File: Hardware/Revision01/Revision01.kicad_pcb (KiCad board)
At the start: 4 copper layers, 100 x 110.1 mm, 91 parts, among them J1 CANBUS backup, J10 StrainConn, J11 StrainConn, J12 StrainConn, J2 Conn_01x02, J3 Conn_01x02, J4 Battery connector, J5 StrainConn, J6 StrainConn, J7 StrainConn, J8 StrainConn, J9 StrainConn, Q1 PMOS, Q2 NMOS, Q3 PMOS, SW1 ON/OFF_SW_SPST_LED, U1 NUCLEO-L476RG, U2 MRF89XAM9AT-I/RM, U3 ICM-45605

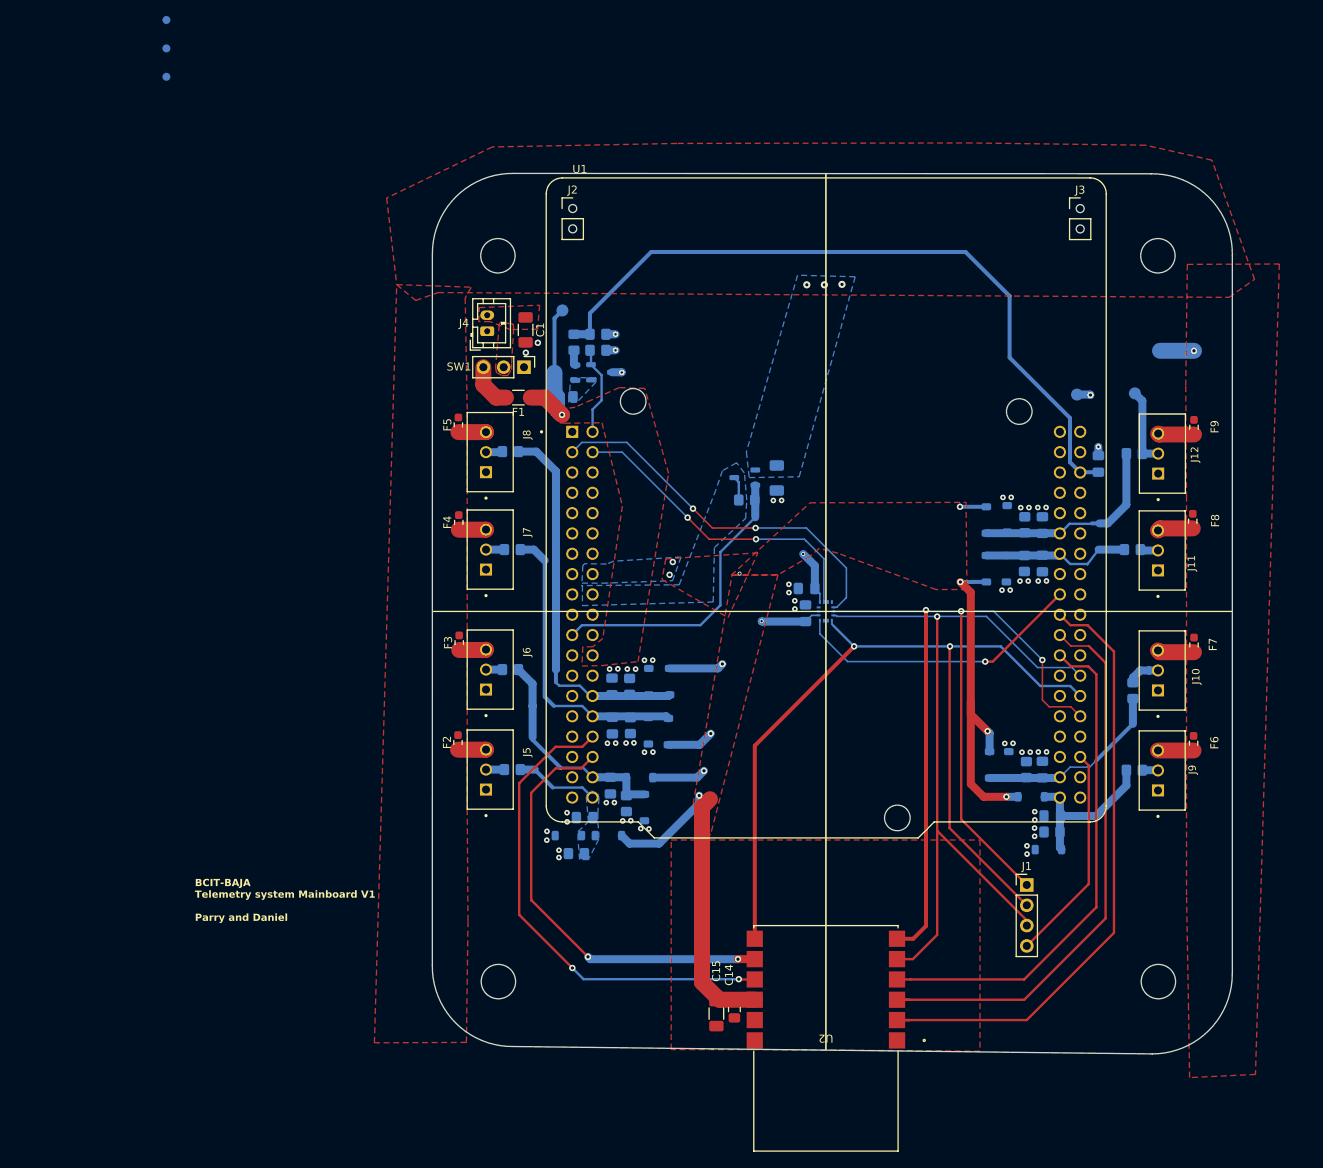
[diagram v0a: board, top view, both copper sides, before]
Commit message: redid ROUTING. Need to redefine layer stackup and stitching via length
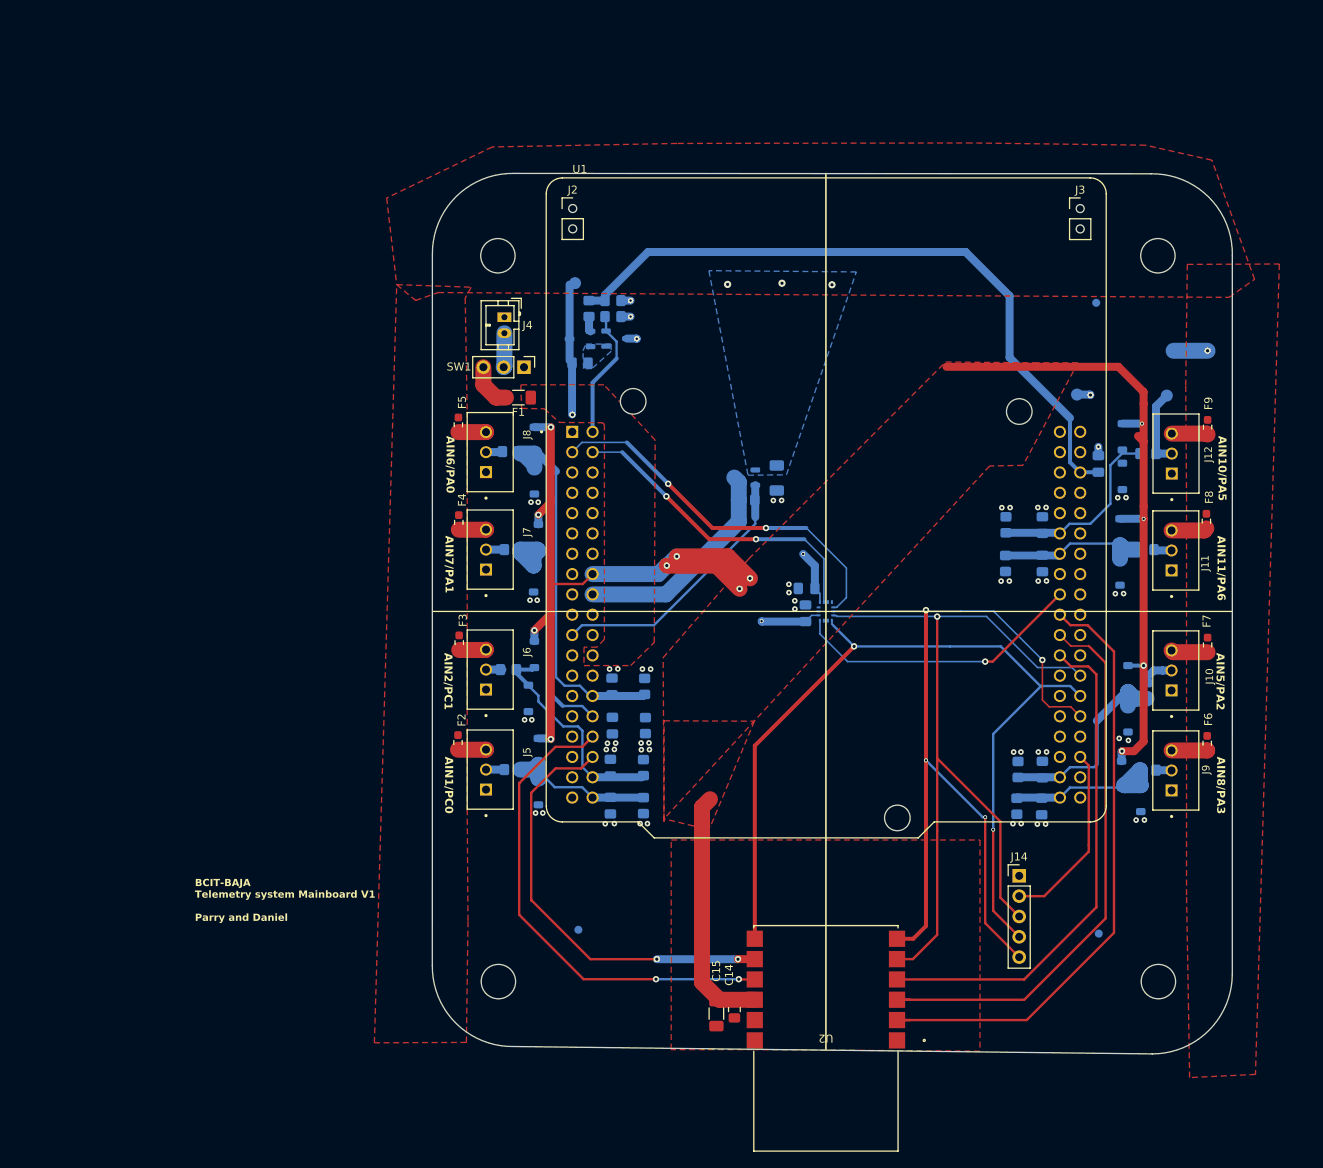
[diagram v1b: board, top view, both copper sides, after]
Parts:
- removed C1: 10uF, Capacitor_SMD:C_1206_3216Metric_Pad1.33x1.80mm_HandSolder
- removed J1: CANBUS backup, Connector_PinHeader_2.54mm:PinHeader_1x04_P2.54mm_Vertical
- added J14: Conn_01x05, Connector_PinHeader_2.54mm:PinHeader_1x05_P2.54mm_Vertical, F.Cu at (184.4, 130.5)
- moved FID2 160.7 mm to (194.3, 137.7)
- moved FID1 121.5 mm to (194.0, 58.8)
- moved FID3 118.4 mm to (129.3, 137.2)
- moved D7 34.6 mm to (123.8, 76.0)
- moved D5 29.2 mm to (124.3, 88.2), turned to -90 degrees
- moved D8 28.9 mm to (123.8, 81.1), turned to -90 degrees
- moved D6 23.8 mm to (123.7, 93.3)
- moved D11 20.4 mm to (198.0, 105.8)
- moved D3 20.3 mm to (123.8, 102.8), turned to -90 degrees
- moved D15 19.9 mm to (197.3, 75.6)
- moved D4 19.9 mm to (123.0, 108.3)
- moved D13 17.3 mm to (197.0, 87.5), turned to -90 degrees
- moved D12 16.0 mm to (198.0, 110.8), turned to -90 degrees
- moved D16 15.3 mm to (197.3, 80.5), turned to -90 degrees
- moved D14 14.2 mm to (197.0, 92.5)
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- renumbered TP10 to +StrainV, TP3 to +Vbatt, TP9 to AIN10, TP8 to GND
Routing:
- net +3.3V: track 124.0 -> 216.1 mm, vias 13 -> 14
- net /PC5_AIN2_14_BATT_V: track 90.5 -> 125.1 mm
- net +5V: track 3.03 -> 27.8 mm
- net /AIN1_1: track 10.5 -> 19.7 mm
- net /PB13_SPI2_SCK: track 120.7 -> 112.7 mm, vias 3 -> 4
- net /PB15_SPI2_MOSI: track 96.6 -> 104.1 mm
- net /BatteryV_Div_Enable_GPIO: track 11.3 -> 16.3 mm
- net /AIN1_7: track 37.2 -> 32.5 mm
- net Net-(BT1-+): track 0.00 -> 4.29 mm
- net /~{CANBUS_CS_GPIO}: track 27.3 -> 23.6 mm
- net /StrainV_Enable_GPIO: track 36.9 -> 33.5 mm
- net /AIN1_6: track 47.1 -> 50.2 mm
- net +V_batt: track 18.7 -> 17.2 mm
- net /AIN1_10: track 25.2 -> 23.8 mm
- net /AIN1_5: track 24.4 -> 25.7 mm
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- removed copper zone on B.Cu, net +3.3V
- removed copper zone on B.Cu, net +5V
- removed copper zone on B.Cu, net /AIN1_1
- removed copper zone on F.Cu, net Net-(BT1-+)
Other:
- board text added: "AIN1/PC0"
- board text added: "AIN10/PA5"
- board text added: "AIN11/PA6"
- board text added: "AIN2/PC1"
- board text added: "AIN5/PA2"
- board text added: "AIN6/PA0"
- board text added: "AIN7/PA1"
- board text added: "AIN8/PA3"

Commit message: forgot to save last commit
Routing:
- net GND: track 6.44 -> 99.3 mm, vias 59 -> 63
- net /AIN1_7: track 32.5 -> 39.2 mm
- net /AIN1_6: track 50.2 -> 56.5 mm
- net /AIN1_10: track 23.8 -> 27.9 mm
- net /ANT_CSDATA_GPIO: track 54.0 -> 54.5 mm
- added copper zone on B.Cu, net GND

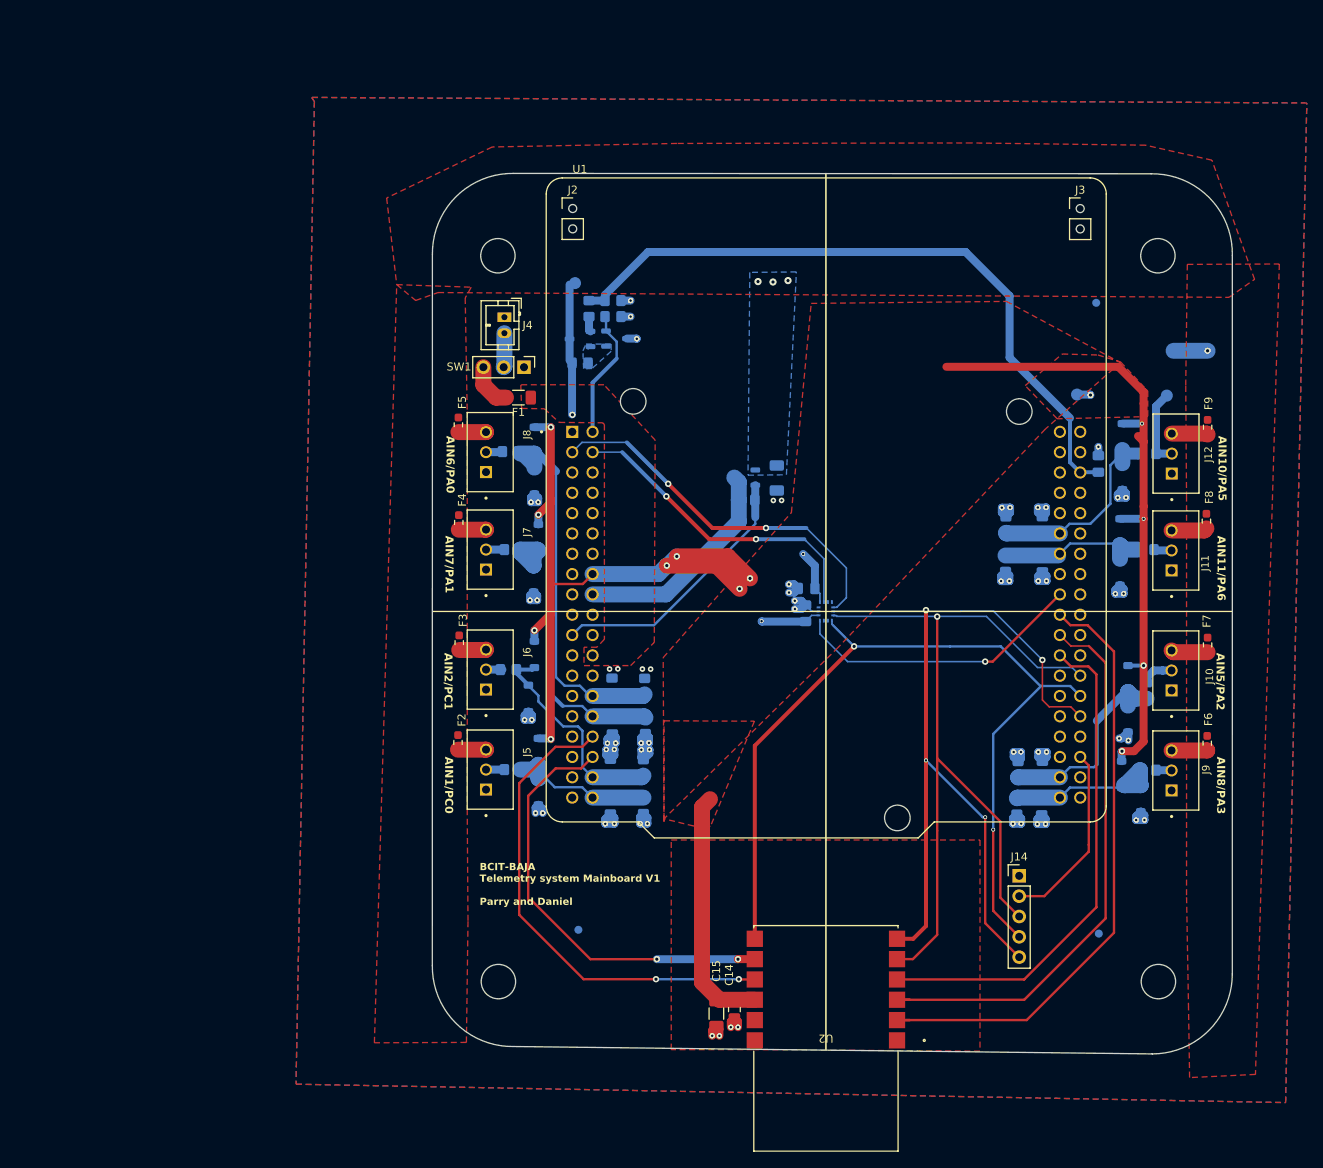
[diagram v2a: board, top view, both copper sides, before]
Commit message: Completion of first routing draft
changed IMU-> MPU9500 due to solderability
initial placement of STITCHING VIA's
Improved silk-screen for strain analog signals
Relabled testpoints
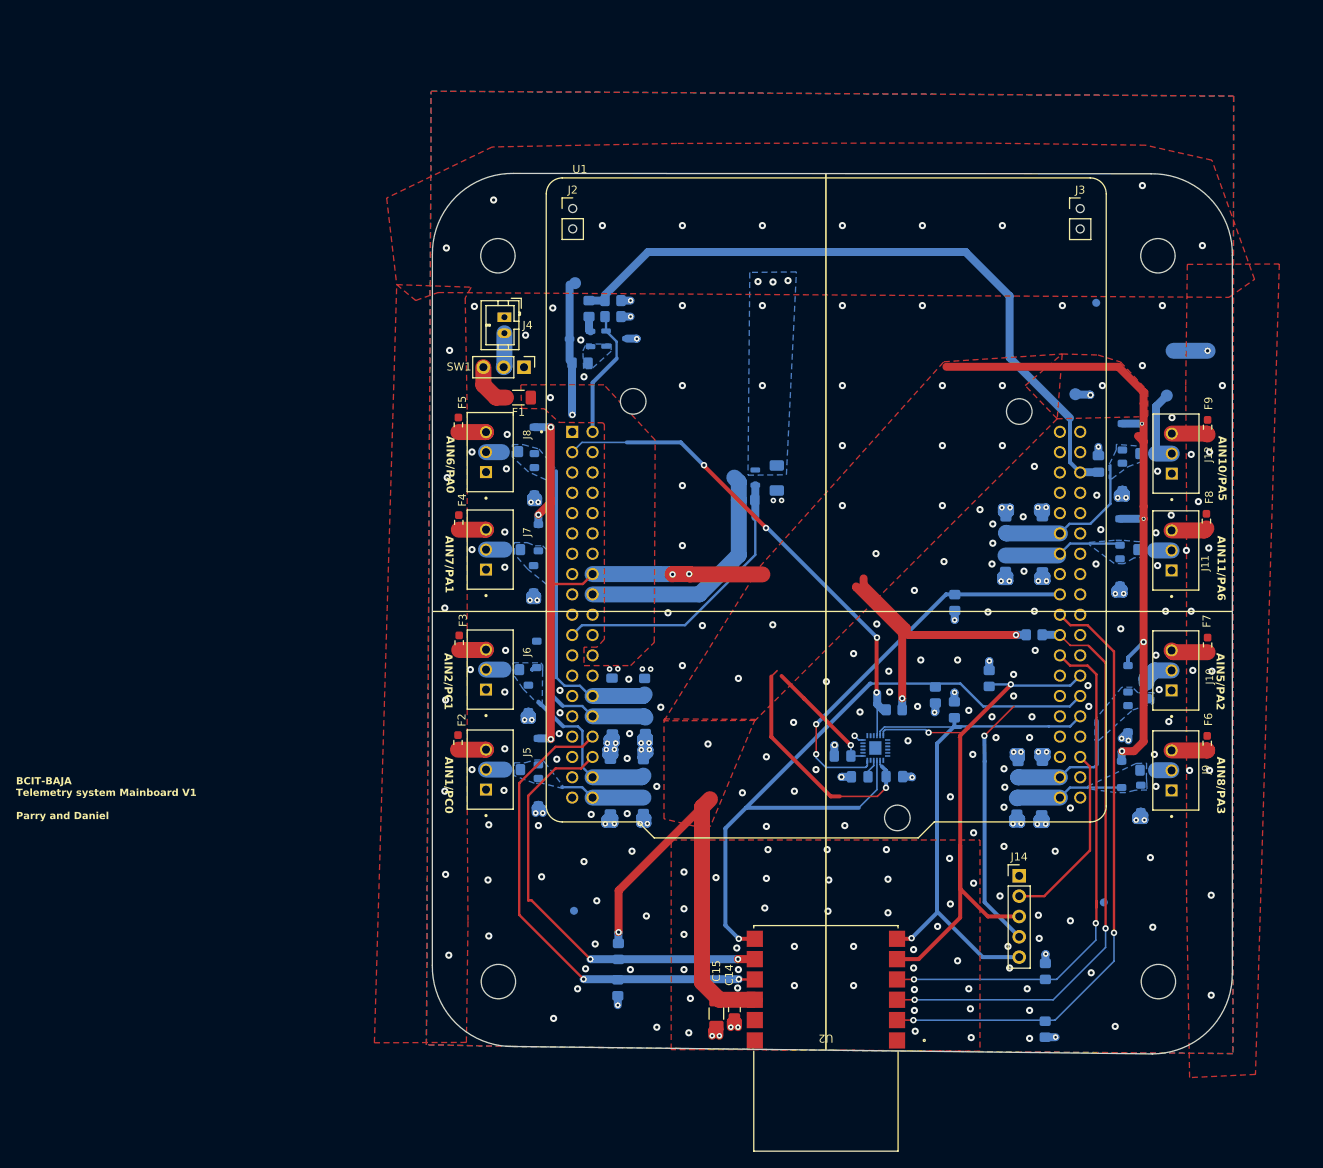
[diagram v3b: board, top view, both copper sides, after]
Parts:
- removed +StrainV: TestPoint, TestPoint:TestPoint_Pad_D1.5mm
- added +VStrain: TestPoint, TestPoint:TestPoint_Pad_D1.5mm, B.Cu at (203.7, 64.9)
- added C1: 0.1uF, Capacitor_SMD:C_0805_2012Metric_Pad1.18x1.45mm_HandSolder, B.Cu at (164.4, 118.1)
- added R33: 10K +-1%, Resistor_SMD:R_0805_2012Metric_Pad1.20x1.40mm_HandSolder, B.Cu at (168.8, 109.7)
- added R34: 10K +-1%, Resistor_SMD:R_0805_2012Metric_Pad1.20x1.40mm_HandSolder, B.Cu at (176.3, 96.3)
- added R35: 10K +-1%, Resistor_SMD:R_0805_2012Metric_Pad1.20x1.40mm_HandSolder, B.Cu at (173.9, 107.9)
- added R36: 10K +-1%, Resistor_SMD:R_0805_2012Metric_Pad1.20x1.40mm_HandSolder, B.Cu at (176.3, 109.7)
- added R37: 10K +-1%, Resistor_SMD:R_0805_2012Metric_Pad1.20x1.40mm_HandSolder, B.Cu at (180.6, 105.8)
- added R38: 10K +-1%, Resistor_SMD:R_0805_2012Metric_Pad1.20x1.40mm_HandSolder, B.Cu at (134.3, 139.9)
- added R39: 10K +-1%, Resistor_SMD:R_0805_2012Metric_Pad1.20x1.40mm_HandSolder, B.Cu at (186.3, 100.3)
- added R40: 10K +-1%, Resistor_SMD:R_0805_2012Metric_Pad1.20x1.40mm_HandSolder, B.Cu at (187.6, 149.6)
- added R41: 10K +-1%, Resistor_SMD:R_0805_2012Metric_Pad1.20x1.40mm_HandSolder, B.Cu at (187.7, 142.4)
- added R42: 10K +-1%, Resistor_SMD:R_0805_2012Metric_Pad1.20x1.40mm_HandSolder, B.Cu at (134.2, 144.5)
- U3: value ICM-45605 -> MPU-6500; footprint ICM-45605:XDCR_ICM-45605 -> MPU-6500:QFN40P300X300X95-25N
- moved C11 23.2 mm to (168.8, 118.1), turned to 0 degrees
- moved C12 21.4 mm to (162.3, 115.5)
- moved U3 18.2 mm to (166.4, 114.5), turned to 180 degrees
- moved FID2 3.95 mm to (195.0, 133.8)
- moved FID3 2.44 mm to (128.7, 134.8)
- moved R2 0.38 mm to (120.9, 104.7)
- moved D3 0.30 mm to (124.1, 102.8)
- moved GND 0.21 mm to (191.4, 70.3)
- renumbered +Vbatt to +V_batt
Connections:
- U1 pad CN10_17: /ICM_INT1_GPIO -> /MPU_INT1_GPIO
- U1 pad CN7_3: /ICM_CS_GPIO -> /MPU_CS_GPIO
- U1 pad CN7_4: /ICM_INT2_GPIO -> unconnected-(U1A-PD2-PadCN7_4)
- U3 pad 1: /PB14_SPI2_MISO -> (no net)
- U3 pad 10: unconnected-(U3-RESV_10-Pad10) -> Net-(U3-REGOUT)
- U3 pad 12: /ICM_CS_GPIO -> /MPU_INT1_GPIO
- U3 pad 13: /PB13_SPI2_SCK -> +3.3V
- U3 pad 14: /PB15_SPI2_MOSI -> (no net)
- U3 pad 2: unconnected-(U3-RESV/MAS_DA-Pad2) -> (no net)
- U3 pad 3: unconnected-(U3-RESV/MAS_CLK-Pad3) -> (no net)
- U3 pad 4: /ICM_INT1_GPIO -> (no net)
- U3 pad 5: +3.3V -> (no net)
- U3 pad 6: GND -> (no net)
- U3 pad 9: /ICM_INT2_GPIO -> /PB14_SPI2_MISO
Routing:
- net +3.3V: track 216.1 -> 299.3 mm
- net /MPU_CS_GPIO: track 0.00 -> 63.9 mm, vias 0 -> 4
- net /MPU_INT1_GPIO: track 0.00 -> 49.9 mm, vias 0 -> 2
- net /ICM_CS_GPIO: track 47.1 -> 0.00 mm, vias 2 -> 0
- net /ICM_INT2_GPIO: track 39.9 -> 0.00 mm, vias 2 -> 0
- net /ICM_INT1_GPIO: track 37.0 -> 0.00 mm, vias 1 -> 0
- net /PB13_SPI2_SCK: track 112.7 -> 78.5 mm, vias 4 -> 1
- net /PB15_SPI2_MOSI: track 104.1 -> 81.4 mm, vias 1 -> 2
- net /AIN1_6: track 56.5 -> 44.5 mm
- net /PB14_SPI2_MISO: track 112.1 -> 123.2 mm
- net /AIN1_5: track 25.7 -> 16.0 mm
- net /AIN1_1: track 19.7 -> 10.8 mm
- net /AIN1_7: track 39.2 -> 30.7 mm
- net /AIN1_10: track 27.9 -> 19.6 mm
- net /AIN1_8: track 20.3 -> 13.6 mm
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- added copper zone on B.Cu, net /AIN1_1
- added copper zone on B.Cu, net /AIN1_10
- added copper zone on B.Cu, net /AIN1_11
- added copper zone on B.Cu, net /AIN1_2
- added copper zone on B.Cu, net /AIN1_5
- added copper zone on B.Cu, net /AIN1_6
- added copper zone on B.Cu, net /AIN1_7
- added copper zone on B.Cu, net /AIN1_8
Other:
- rule pad_to_mask_clearance: 0 -> 0.08
